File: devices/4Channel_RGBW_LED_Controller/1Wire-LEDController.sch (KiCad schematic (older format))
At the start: 35 parts, among them CON1 BARREL_JACK, J1 RJ45, J2 RJ45, J3 JACK_STEREO, P1 CONN_02X05, P2 CONN_01X05, P3 CONN_01X05, P4 DC_IN, P5 CONN_01X05, P6 CONN_01X05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

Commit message: Big cleanup/upgrade of Kicad files
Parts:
- C1: symbol CP -> Device:CP
- C2, C3, C4, C5: symbol C -> Device:C
- CON1: symbol BARREL_JACK -> conn:BARREL_JACK
- J1, J2: symbol RJ45 -> conn:RJ45
- J3: symbol JACK_STEREO -> 1Wire-LEDController-rescue:JACK_STEREO
- P1: symbol CONN_02X05 -> conn:CONN_02X05
- P2, P3, P5, P6, P7: symbol CONN_01X05 -> conn:CONN_01X05
- P4: symbol CONN_01X02 -> conn:CONN_01X02
- Q1, Q10, Q11, Q12, Q13, Q14, Q15, Q16, Q2, Q3, Q4, Q5, Q6, Q7, Q8, Q9: symbol Q_NMOS_GDS -> Device:Q_NMOS_GDS
- R1: symbol R -> Device:R
- U1: symbol LP2950 -> 1Wire-LEDController-rescue:LP2950
- U2: symbol STM32F030R8 -> automotive-light-controller-cache:STM32F030R8

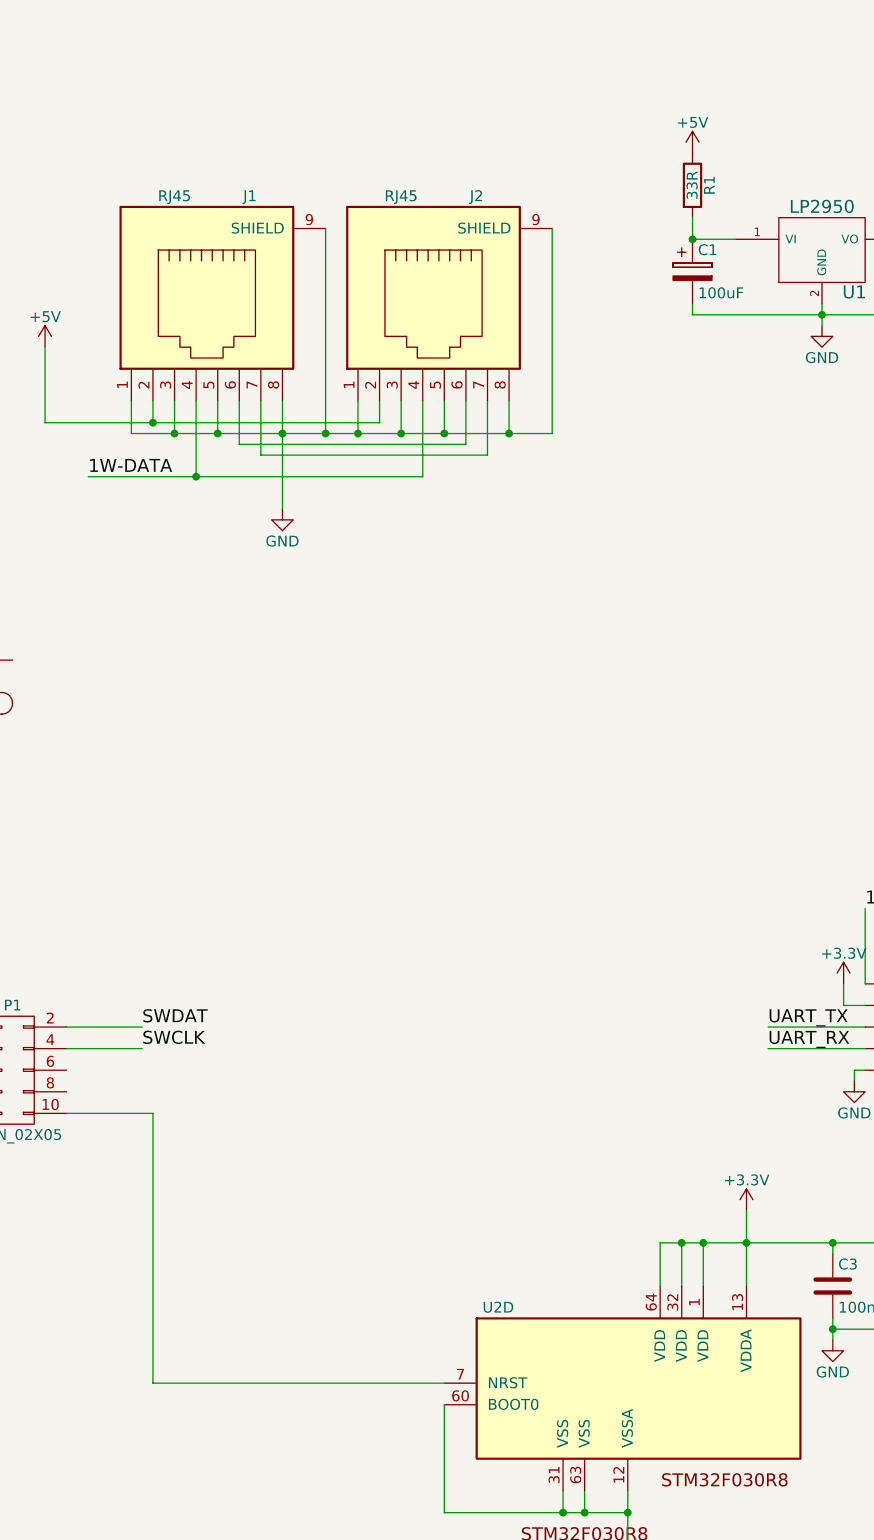
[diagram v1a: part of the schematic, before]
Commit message: Bump all active boards to Revision 1.2
- Remove dropping resistor from 5V power line
- Add pullup resistor to Reset line
- Add pin markings to STM32 chip footprint

Signed-off-by: Alastair D'Silva <alastair@d-silva.org>
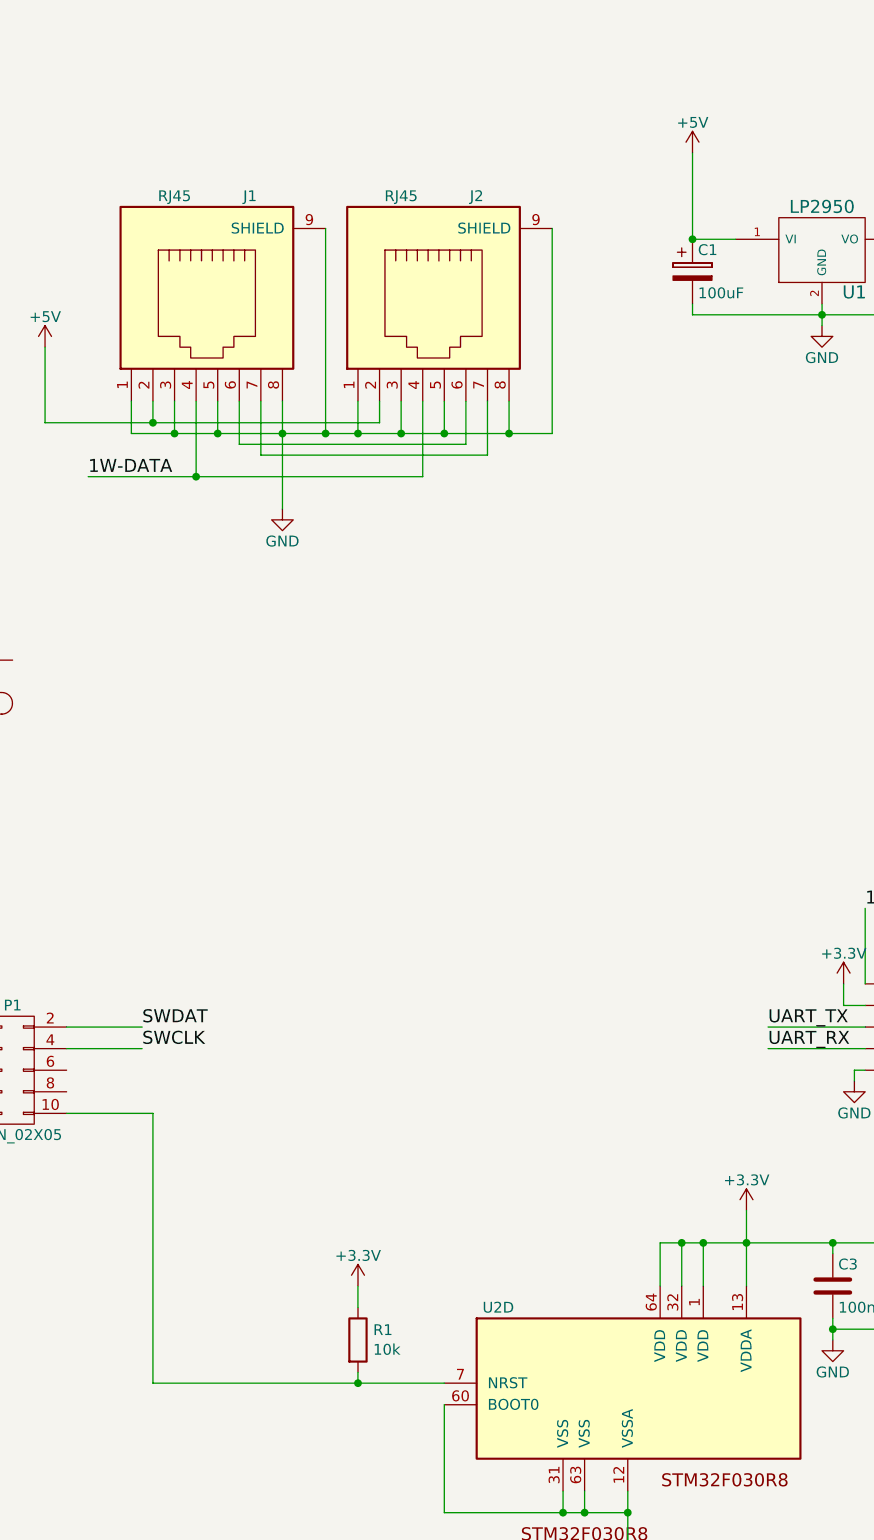
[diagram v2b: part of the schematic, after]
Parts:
- R1: value 33R -> 10k
- U2: footprint LQFP-64 -> Housings_QFP:LQFP-64_10x10mm_Pitch0.5mm
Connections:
- net +3V3: now also R1.1
- net +5V: now also C1.1, U1.1 (VI); no longer R1.1
- net at P1.10 (P10), U2.7 (NRST): now also R1.2
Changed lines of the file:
@@
 Sheet 1 1
 Title "1 Wire LED Controller"
-Date "2017-03-09"
-Rev "1.0"
+Date "2018-12-23"
+Rev "1.2"
 Comp "Inferno Embedded"
 Comment1 "Licensed under the TAPR Open Hardware License (www.tapr.org/OHL)"
-Comment2 "Copyright © 2017 Inferno Embedded"
+Comment2 "Copyright © 2018 Inferno Embedded"
 Comment3 ""
 Comment4 ""
@@
 Wire Wire Line
 	14450 3400 14250 3400
-Wire Wire Line
-	14250 3400 14250 3300
 $Comp
 L Device:CP C1
@@
 Connection ~ 13650 9300
 Wire Wire Line
-	11750 8700 13100 8700
+	11750 8700 12700 8700
 Wire Wire Line
 	11750 7450 11750 8700
@@
 Connection ~ 14250 3400
 Connection ~ 15350 3400
-$Comp
-L Device:R R1
-U 1 1 58B28CDC
-P 14250 3150
-F 0 "R1" V 14330 3150 50  0000 C CNN
-F 1 "33R" V 14250 3150 50  0000 C CNN
-F 2 "Resistors_SMD:R_0603" V 14180 3150 50  0001 C CNN
-F 3 "" H 14250 3150 50  0000 C CNN
-	1    14250 3150
-	1    0    0    -1
-$EndComp
 $Comp
 L conn:CONN_01X05 P6
@@
 F 0 "U2" H 1300 1700 50  0000 C CNN
 F 1 "STM32F030R8" H 1500 1800 50  0001 C CNN
-F 2 "LQFP-64" H 1400 1900 50  0001 C CIN
+F 2 "Housings_QFP:LQFP-64_10x10mm_Pitch0.5mm" H 1400 1900 50  0001 C CIN
 F 3 "" H 4500 -850 50  0000 C CNN
 	2    1200 1650
@@
 Wire Wire Line
 	7400 2750 8050 2750
+Wire Wire Line
+	14250 3000 14250 3400
+$Comp
+L power:+3.3V #PWR025
+U 1 1 5C2096B6
+P 12700 8250
+F 0 "#PWR025" H 12700 8100 50  0001 C CNN
+F 1 "+3.3V" H 12700 8390 50  0000 C CNN
+F 2 "" H 12700 8250 50  0000 C CNN
+F 3 "" H 12700 8250 50  0000 C CNN
+	1    12700 8250
+	1    0    0    -1
+$EndComp
+$Comp
+L Device:R R1
+U 1 1 5C2098E5
+P 12700 8500
+F 0 "R1" H 12770 8546 50  0000 L CNN
+F 1 "10k" H 12770 8455 50  0000 L CNN
+F 2 "Resistors_SMD:R_0603" V 12630 8500 50  0001 C CNN
+F 3 "~" H 12700 8500 50  0001 C CNN
+	1    12700 8500
+	1    0    0    -1
+$EndComp
+Wire Wire Line
+	12700 8700 12700 8650
+Connection ~ 12700 8700
+Wire Wire Line
+	12700 8700 13100 8700
+Wire Wire Line
+	12700 8350 12700 8250
 $EndSCHEMATC
